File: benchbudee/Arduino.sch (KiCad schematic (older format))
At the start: 0 parts

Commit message: Setting up for layout
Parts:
- added ARD?: ARDUINO_PINS, symbol ARDUINO_PINS
- added R? (x17): R, symbol R
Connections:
- net MISO: now also R?.1
- net MOSI: now also R?.1
- net SCLK: now also R?.1
- new net: ARD?.1 (5V), R?.1
- new net: ARD?.11 (GPIO0), R?.2
- new net: ARD?.12 (GPIO1), R?.2
- new net: ARD?.18 (GPIO7), R?.2
- new net: ARD?.19 (GPIO8), R?.2
- new net: ARD?.2 (GND), R?.1
- new net: ARD?.20 (PWM0), R?.2
- new net: ARD?.21 (CS_N), R?.2
- new net: ARD?.22 (MOSI), R?.2
- new net: ARD?.23 (MISO), R?.2
- new net: ARD?.24 (SCK), R?.2
- new net: ARD?.3 (GND), R?.1
- new net: ARD?.4 (9V), R?.1
- new net: ARD?.5 (AIN0), R?.1
- new net: ARD?.6 (AIN1), R?.1
- new net: ARD?.7 (AIN2), R?.1
- new net: ARD?.8 (AIN3), R?.1
- new net +12P: R?.2
- new net +5V: R?.2
- new net CURR_MEAS: R?.2
- new net FAN_CS_N: R?.1
- new net FAN_MODE: R?.1
- new net FAN_PWM: R?.1
- new net GND: R?.2, R?.2
- new net LED_EN_PWM: R?.1
- new net RELAY+: R?.1
- new net TACH_MEAS: R?.2
- new net TC_CS_N: R?.1
- new net V+_ADJ_MON: R?.2
- new net V-_ADJ_MON: R?.2

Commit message: Relay module footprints done
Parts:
- gave numbers to parts that had none: 18
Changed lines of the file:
@@
 TACH_MEAS
 $Comp
-L ARDUINO_PINS ARD?
+L ARDUINO_PINS ARD1
 U 1 1 53206000
 P 5700 3550
-F 0 "ARD?" H 5700 2250 60  0000 C CNN
+F 0 "ARD1" H 5700 2250 60  0000 C CNN
 F 1 "ARDUINO_PINS" H 5700 3600 60  0000 C CNN
 F 2 "" H 5200 4300 60  0000 C CNN
@@
 CURR_MEAS
 $Comp
-L R R?
+L R R38
 U 1 1 53206503
 P 7150 3200
-F 0 "R?" V 7230 3200 40  0000 C CNN
+F 0 "R38" V 7230 3200 40  0000 C CNN
 F 1 "R" V 7157 3201 40  0000 C CNN
 F 2 "" V 7080 3200 30  0000 C CNN
@@
 	7400 3200 7600 3200
 $Comp
-L R R?
+L R R42
 U 1 1 53206A18
 P 7150 4550
-F 0 "R?" V 7230 4550 40  0000 C CNN
+F 0 "R42" V 7230 4550 40  0000 C CNN
 F 1 "R" V 7157 4551 40  0000 C CNN
 F 2 "" V 7080 4550 30  0000 C CNN
@@
 	7400 4550 7600 4550
 $Comp
-L GND #PWR?
+L GND #PWR053
 U 1 1 53206A3A
 P 8650 4900
-F 0 "#PWR?" H 8650 4900 30  0001 C CNN
+F 0 "#PWR053" H 8650 4900 30  0001 C CNN
 F 1 "GND" H 8650 4830 30  0001 C CNN
 F 2 "" H 8650 4900 60  0000 C CNN
@@
 	8650 4550 8650 4900
 $Comp
-L R R?
+L R R34
 U 1 1 53206A58
 P 4300 3500
-F 0 "R?" V 4380 3500 40  0000 C CNN
+F 0 "R34" V 4380 3500 40  0000 C CNN
 F 1 "R" V 4307 3501 40  0000 C CNN
 F 2 "" V 4230 3500 30  0000 C CNN
@@
 $EndComp
 $Comp
-L R R?
+L R R33
 U 1 1 53206A63
 P 4300 3350
-F 0 "R?" V 4380 3350 40  0000 C CNN
+F 0 "R33" V 4380 3350 40  0000 C CNN
 F 1 "R" V 4307 3351 40  0000 C CNN
 F 2 "" V 4230 3350 30  0000 C CNN
@@
 V-_ADJ_MON
 $Comp
-L R R?
+L R R32
 U 1 1 53207FED
 P 4300 3200
-F 0 "R?" V 4380 3200 40  0000 C CNN
+F 0 "R32" V 4380 3200 40  0000 C CNN
 F 1 "R" V 4307 3201 40  0000 C CNN
 F 2 "" V 4230 3200 30  0000 C CNN
@@
 $EndComp
 $Comp
-L R R?
+L R R31
 U 1 1 53207FF8
 P 4300 3050
-F 0 "R?" V 4380 3050 40  0000 C CNN
+F 0 "R31" V 4380 3050 40  0000 C CNN
 F 1 "R" V 4307 3051 40  0000 C CNN
 F 2 "" V 4230 3050 30  0000 C CNN
@@
 	4700 3200 4550 3200
 $Comp
-L R R?
+L R R35
 U 1 1 5320805A
 P 7150 2750
-F 0 "R?" V 7230 2750 40  0000 C CNN
+F 0 "R35" V 7230 2750 40  0000 C CNN
 F 1 "R" V 7157 2751 40  0000 C CNN
 F 2 "" V 7080 2750 30  0000 C CNN
@@
 $EndComp
 $Comp
-L R R?
+L R R36
 U 1 1 53208065
 P 7150 2900
-F 0 "R?" V 7230 2900 40  0000 C CNN
+F 0 "R36" V 7230 2900 40  0000 C CNN
 F 1 "R" V 7157 2901 40  0000 C CNN
 F 2 "" V 7080 2900 30  0000 C CNN
@@
 $EndComp
 $Comp
-L R R?
+L R R37
 U 1 1 53208070
 P 7150 3050
-F 0 "R?" V 7230 3050 40  0000 C CNN
+F 0 "R37" V 7230 3050 40  0000 C CNN
 F 1 "R" V 7157 3051 40  0000 C CNN
 F 2 "" V 7080 3050 30  0000 C CNN
@@
 $EndComp
 $Comp
-L R R?
+L R R41
 U 1 1 5320807B
 P 7150 3650
-F 0 "R?" V 7230 3650 40  0000 C CNN
+F 0 "R41" V 7230 3650 40  0000 C CNN
 F 1 "R" V 7157 3651 40  0000 C CNN
 F 2 "" V 7080 3650 30  0000 C CNN
@@
 LED_EN_PWM
 $Comp
-L R R?
+L R R39
 U 1 1 53208124
 P 7150 3350
-F 0 "R?" V 7230 3350 40  0000 C CNN
+F 0 "R39" V 7230 3350 40  0000 C CNN
 F 1 "R" V 7157 3351 40  0000 C CNN
 F 2 "" V 7080 3350 30  0000 C CNN
@@
 TC_CS_N
 $Comp
-L R R?
+L R R40
 U 1 1 532188BC
 P 7150 3500
-F 0 "R?" V 7230 3500 40  0000 C CNN
+F 0 "R40" V 7230 3500 40  0000 C CNN
 F 1 "R" V 7157 3501 40  0000 C CNN
 F 2 "" V 7080 3500 30  0000 C CNN
@@
 FAN_MODE
 $Comp
-L R R?
+L R R43
 U 1 1 53262459
 P 7150 4700
-F 0 "R?" V 7230 4700 40  0000 C CNN
+F 0 "R43" V 7230 4700 40  0000 C CNN
 F 1 "R" V 7157 4701 40  0000 C CNN
 F 2 "" V 7080 4700 30  0000 C CNN
@@
 	6900 4700 6700 4700
 $Comp
-L R R?
+L R R30
 U 1 1 532624A4
 P 4300 2900
-F 0 "R?" V 4380 2900 40  0000 C CNN
+F 0 "R30" V 4380 2900 40  0000 C CNN
 F 1 "R" V 4307 2901 40  0000 C CNN
 F 2 "" V 4230 2900 30  0000 C CNN
@@
 	3150 2900 4050 2900
 $Comp
-L +12P #PWR?
+L +12P #PWR054
 U 1 1 53262502
 P 3150 2800
-F 0 "#PWR?" H 3150 2770 30  0001 C CNN
+F 0 "#PWR054" H 3150 2770 30  0001 C CNN
 F 1 "+12P" H 3150 2900 30  0000 C CNN
 F 2 "" H 3150 2800 60  0000 C CNN
@@
 $EndComp
 $Comp
-L +5V #PWR?
+L +5V #PWR055
 U 1 1 5356A2B2
 P 3150 2300
-F 0 "#PWR?" H 3150 2390 20  0001 C CNN
+F 0 "#PWR055" H 3150 2390 20  0001 C CNN
 F 1 "+5V" H 3150 2390 30  0000 C CNN
 F 2 "" H 3150 2300 60  0000 C CNN
@@
 	3150 2300 3150 2450
 $Comp
-L GND #PWR?
+L GND #PWR056
 U 1 1 5356A2E7
 P 3600 2750
-F 0 "#PWR?" H 3600 2750 30  0001 C CNN
+F 0 "#PWR056" H 3600 2750 30  0001 C CNN
 F 1 "GND" H 3600 2680 30  0001 C CNN
 F 2 "" H 3600 2750 60  0000 C CNN
@@
 $EndComp
 $Comp
-L R R?
+L R R28
 U 1 1 5356A2F9
 P 4300 2600
-F 0 "R?" V 4380 2600 40  0000 C CNN
+F 0 "R28" V 4380 2600 40  0000 C CNN
 F 1 "R" V 4307 2601 40  0000 C CNN
 F 2 "" V 4230 2600 30  0000 C CNN
@@
 $EndComp
 $Comp
-L R R?
+L R R29
 U 1 1 5356A304
 P 4300 2750
-F 0 "R?" V 4380 2750 40  0000 C CNN
+F 0 "R29" V 4380 2750 40  0000 C CNN
 F 1 "R" V 4307 2751 40  0000 C CNN
 F 2 "" V 4230 2750 30  0000 C CNN
@@
 $EndComp
 $Comp
-L R R?
+L R R27
 U 1 1 5356A30F
 P 4300 2450
-F 0 "R?" V 4380 2450 40  0000 C CNN
+F 0 "R27" V 4380 2450 40  0000 C CNN
 F 1 "R" V 4307 2451 40  0000 C CNN
 F 2 "" V 4230 2450 30  0000 C CNN

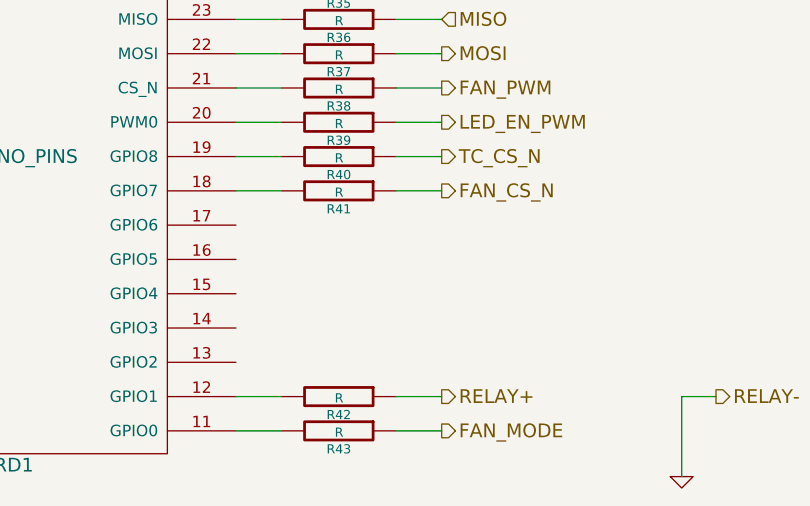
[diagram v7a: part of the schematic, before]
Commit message: Schematic and associations for the thermocouple module
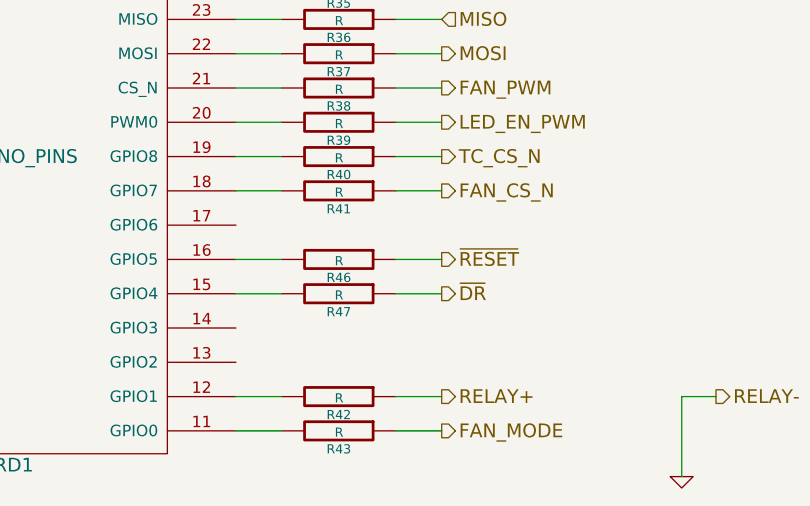
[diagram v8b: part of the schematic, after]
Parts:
- added R46, R47: R, symbol R
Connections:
- net at ARD1.15 (GPIO4): now also R47.2
- net at ARD1.16 (GPIO5): now also R46.2
- new net ~DR: R47.1
- new net ~RESET: R46.1
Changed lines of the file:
@@
 	7400 4550 7600 4550
 $Comp
-L GND #PWR053
+L GND #PWR061
 U 1 1 53206A3A
 P 8650 4900
-F 0 "#PWR053" H 8650 4900 30  0001 C CNN
+F 0 "#PWR061" H 8650 4900 30  0001 C CNN
 F 1 "GND" H 8650 4830 30  0001 C CNN
 F 2 "" H 8650 4900 60  0000 C CNN
@@
 	3150 2900 4050 2900
 $Comp
-L +12P #PWR054
+L +12P #PWR062
 U 1 1 53262502
 P 3150 2800
-F 0 "#PWR054" H 3150 2770 30  0001 C CNN
+F 0 "#PWR062" H 3150 2770 30  0001 C CNN
 F 1 "+12P" H 3150 2900 30  0000 C CNN
 F 2 "" H 3150 2800 60  0000 C CNN
@@
 $EndComp
 $Comp
-L +5V #PWR055
+L +5V #PWR063
 U 1 1 5356A2B2
 P 3150 2300
-F 0 "#PWR055" H 3150 2390 20  0001 C CNN
+F 0 "#PWR063" H 3150 2390 20  0001 C CNN
 F 1 "+5V" H 3150 2390 30  0000 C CNN
 F 2 "" H 3150 2300 60  0000 C CNN
@@
 	3150 2300 3150 2450
 $Comp
-L GND #PWR056
+L GND #PWR064
 U 1 1 5356A2E7
 P 3600 2750
-F 0 "#PWR056" H 3600 2750 30  0001 C CNN
+F 0 "#PWR064" H 3600 2750 30  0001 C CNN
 F 1 "GND" H 3600 2680 30  0001 C CNN
 F 2 "" H 3600 2750 60  0000 C CNN
@@
 	3800 2750 3800 2600
 Connection ~ 3800 2600
+Text HLabel 7600 3950 2    60   Output ~ 0
+~RESET
+$Comp
+L R R46
+U 1 1 535F6093
+P 7150 3950
+F 0 "R46" V 7230 3950 40  0000 C CNN
+F 1 "R" V 7157 3951 40  0000 C CNN
+F 2 "" V 7080 3950 30  0000 C CNN
+F 3 "" H 7150 3950 30  0000 C CNN
+	1    7150 3950
+	0    1    1    0
+$EndComp
+Wire Wire Line
+	6700 3950 6900 3950
+Wire Wire Line
+	7400 3950 7600 3950
+Text HLabel 7600 4100 2    60   Output ~ 0
+~DR
+$Comp
+L R R47
+U 1 1 535F609C
+P 7150 4100
+F 0 "R47" V 7230 4100 40  0000 C CNN
+F 1 "R" V 7157 4101 40  0000 C CNN
+F 2 "" V 7080 4100 30  0000 C CNN
+F 3 "" H 7150 4100 30  0000 C CNN
+	1    7150 4100
+	0    1    1    0
+$EndComp
+Wire Wire Line
+	6700 4100 6900 4100
+Wire Wire Line
+	7400 4100 7600 4100
 $EndSCHEMATC
